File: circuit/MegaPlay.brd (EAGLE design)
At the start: 38.1 x 45.7 mm, 13 parts, among them IC1 4052N, IC2 4052N, M1 ARDUINO-NANO-3.0, X1 Mega, X2 5200

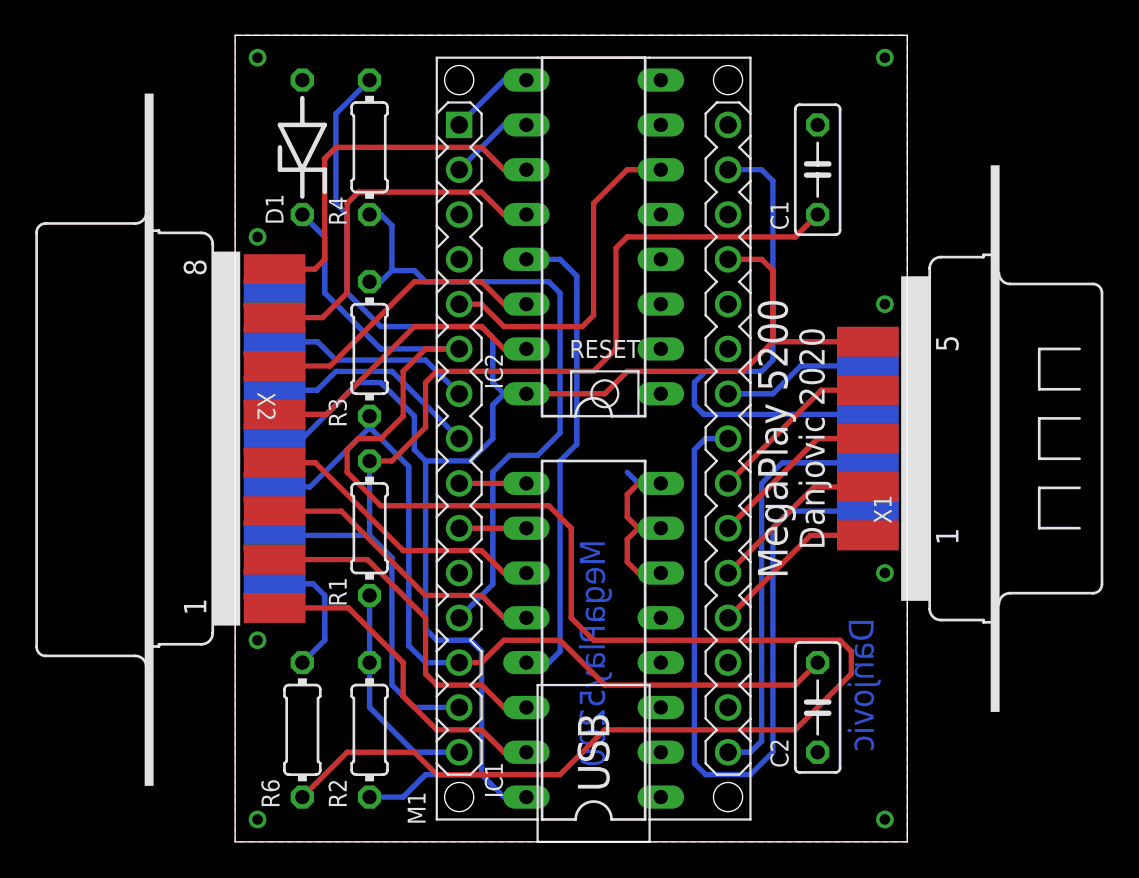
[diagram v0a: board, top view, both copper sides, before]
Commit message: Added decoupling capacitor to Analog Switches power supply.
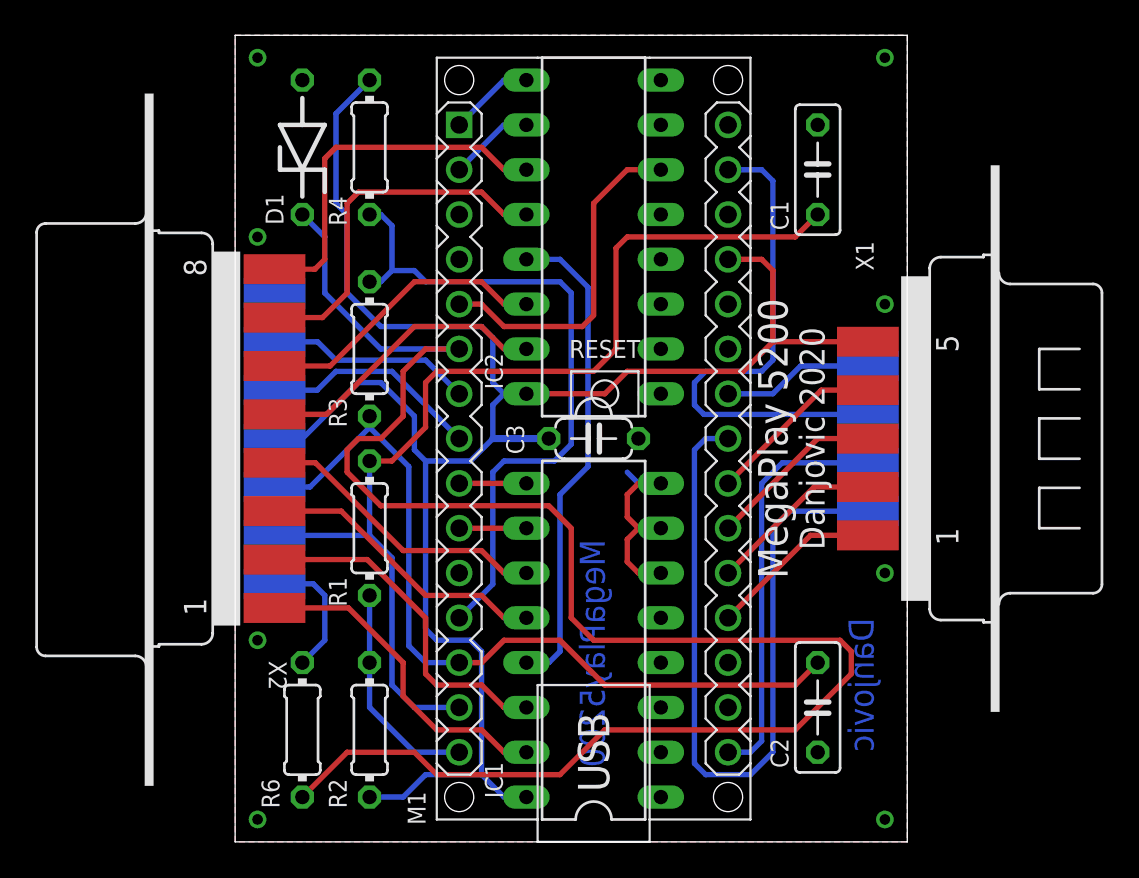
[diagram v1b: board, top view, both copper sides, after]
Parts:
- added C3: 100n, rcl:C050-024X044
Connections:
- net +5V: now also C3.1
- net GND: now also C3.2
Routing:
- net +5V: track 104.7 -> 107.8 mm
- net N$1: track 37.4 -> 39.0 mm
- net N$3: track 27.1 -> 27.6 mm
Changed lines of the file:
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@@
 <grid distance="0.025" unitdist="inch" unit="inch" style="lines" multiple="1" display="no" altdistance="0.0125" altunitdist="inch" altunit="inch"/>
 <layers>
-<layer number="1" name="Top" color="4" fill="1" visible="yes" active="yes"/>
-<layer number="16" name="Bottom" color="1" fill="1" visible="yes" active="yes"/>
+<layer number="1" name="Top" color="4" fill="1" visible="no" active="yes"/>
+<layer number="16" name="Bottom" color="1" fill="1" visible="no" active="yes"/>
 <layer number="17" name="Pads" color="2" fill="1" visible="yes" active="yes"/>
 <layer number="18" name="Vias" color="2" fill="1" visible="yes" active="yes"/>
@@
 <layer number="27" name="tValues" color="7" fill="1" visible="yes" active="yes"/>
 <layer number="28" name="bValues" color="7" fill="1" visible="no" active="yes"/>
-<layer number="29" name="tStop" color="7" fill="3" visible="no" active="yes"/>
+<layer number="29" name="tStop" color="7" fill="3" visible="yes" active="yes"/>
 <layer number="30" name="bStop" color="7" fill="6" visible="no" active="yes"/>
 <layer number="31" name="tCream" color="7" fill="4" visible="no" active="yes"/>
@@
 <attribute name="MPN" value="" x="41.91" y="22.86" size="1.778" layer="27" rot="R270" display="off"/>
 <attribute name="OC_FARNELL" value="unknown" x="41.91" y="22.86" size="1.778" layer="27" rot="R270" display="off"/>
-<attribute name="NAME" x="36.195" y="19.685" size="1.016" layer="25" ratio="10" rot="R270"/>
-<attribute name="VALUE" x="36.195" y="24.13" size="1.016" layer="27" ratio="10" rot="R270"/>
+<attribute name="NAME" x="36.195" y="32.385" size="1.016" layer="25" ratio="10" rot="R90"/>
+<attribute name="VALUE" x="37.465" y="32.385" size="1.016" layer="27" ratio="10" rot="R90"/>
 </element>
 <element name="X2" library="con-subd" package="F15D" value="5200" x="-3.81" y="22.86" smashed="yes" rot="R90">
@@
 <attribute name="MPN" value="" x="-3.81" y="22.86" size="1.778" layer="27" rot="R90" display="off"/>
 <attribute name="OC_FARNELL" value="unknown" x="-3.81" y="22.86" size="1.778" layer="27" rot="R90" display="off"/>
-<attribute name="NAME" x="1.27" y="25.5016" size="1.016" layer="25" ratio="10" rot="SR270"/>
-<attribute name="VALUE" x="1.27" y="22.3266" size="1.016" layer="27" ratio="10" rot="SR270"/>
+<attribute name="NAME" x="1.905" y="10.2616" size="1.016" layer="25" ratio="10" rot="SR270"/>
+<attribute name="VALUE" x="0.635" y="10.2616" size="1.016" layer="27" ratio="10" rot="SR270"/>
 </element>
 <element name="M1" library="diy-modules" package="ARDUINO-NANO-3.0" value="ARDUINO-NANO-3.0" x="20.32" y="22.86" smashed="yes" rot="R90">
@@
 <attribute name="NAME" x="2.7432" y="34.9758" size="1.016" layer="25" ratio="10" rot="R90"/>
 <attribute name="VALUE" x="2.413" y="41.275" size="1.016" layer="27" ratio="10" rot="R90"/>
+</element>
+<element name="C3" library="rcl" package="C050-024X044" value="100n" x="20.32" y="22.86" smashed="yes">
+<attribute name="NAME" x="16.383" y="21.971" size="1.016" layer="25" ratio="10" rot="R90"/>
+<attribute name="VALUE" x="24.892" y="21.336" size="1.016" layer="27" ratio="10" rot="R90"/>
 </element>
 </elements>
@@
 <contactref element="IC2" pad="3"/>
 <contactref element="D1" pad="A"/>
+<contactref element="C3" pad="2"/>
 </signal>
 <signal name="N$12">
@@
 <wire x1="30.48" y1="32.385" x2="29.845" y2="33.02" width="0.3048" layer="1"/>
 <wire x1="28.8038" y1="26.67" x2="30.48" y2="28.3462" width="0.3048" layer="1"/>
+<contactref element="C3" pad="1"/>
+<wire x1="17.78" y1="22.86" x2="14.605" y2="22.86" width="0.4064" layer="16"/>
 </signal>
 <signal name="VIN">
@@
 <wire x1="8.89" y1="34.925" x2="8.89" y2="32.385" width="0.3048" layer="16"/>
 <wire x1="14.605" y1="14.605" x2="14.605" y2="20.955" width="0.3048" layer="16"/>
-<wire x1="14.605" y1="20.955" x2="15.5575" y2="21.9075" width="0.3048" layer="16"/>
-<wire x1="15.5575" y1="21.9075" x2="17.145" y2="21.9075" width="0.3048" layer="16"/>
-<wire x1="17.145" y1="21.9075" x2="18.415" y2="23.1775" width="0.3048" layer="16"/>
-<wire x1="18.415" y1="23.1775" x2="18.415" y2="31.115" width="0.3048" layer="16"/>
-<wire x1="18.415" y1="31.115" x2="17.78" y2="31.75" width="0.3048" layer="16"/>
-<wire x1="17.78" y1="31.75" x2="10.795" y2="31.75" width="0.3048" layer="16"/>
+<wire x1="14.605" y1="20.955" x2="15.24" y2="21.59" width="0.3048" layer="16"/>
+<wire x1="15.24" y1="21.59" x2="18.0975" y2="21.59" width="0.3048" layer="16"/>
+<wire x1="18.0975" y1="21.59" x2="19.05" y2="22.5425" width="0.3048" layer="16"/>
+<wire x1="19.05" y1="22.5425" x2="19.05" y2="31.115" width="0.3048" layer="16"/>
+<wire x1="19.05" y1="31.115" x2="18.415" y2="31.75" width="0.3048" layer="16"/>
+<wire x1="18.415" y1="31.75" x2="10.795" y2="31.75" width="0.3048" layer="16"/>
 <wire x1="10.795" y1="31.75" x2="10.16" y2="32.385" width="0.3048" layer="16"/>
 <wire x1="10.16" y1="32.385" x2="8.89" y2="32.385" width="0.3048" layer="16"/>
@@
 <contactref element="IC2" pad="13"/>
 <wire x1="16.51" y1="33.02" x2="18.415" y2="33.02" width="0.3048" layer="16"/>
-<wire x1="18.415" y1="33.02" x2="19.3675" y2="32.0675" width="0.3048" layer="16"/>
-<wire x1="19.3675" y1="32.0675" x2="19.3675" y2="22.5425" width="0.3048" layer="16"/>
-<wire x1="19.3675" y1="22.5425" x2="18.415" y2="21.59" width="0.3048" layer="16"/>
-<wire x1="18.415" y1="21.59" x2="18.415" y2="10.795" width="0.3048" layer="16"/>
+<wire x1="18.415" y1="33.02" x2="20.0025" y2="31.4325" width="0.3048" layer="16"/>
+<wire x1="20.0025" y1="31.4325" x2="20.0025" y2="21.2725" width="0.3048" layer="16"/>
+<wire x1="20.0025" y1="21.2725" x2="18.415" y2="19.685" width="0.3048" layer="16"/>
+<wire x1="18.415" y1="19.685" x2="18.415" y2="10.795" width="0.3048" layer="16"/>
 <wire x1="18.415" y1="10.795" x2="17.78" y2="10.16" width="0.3048" layer="16"/>
 <wire x1="17.78" y1="10.16" x2="16.51" y2="10.16" width="0.3048" layer="16"/>
